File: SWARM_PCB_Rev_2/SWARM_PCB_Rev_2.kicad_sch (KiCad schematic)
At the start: 4 parts, among them J25 Conn_01x12_Pin, J26 Conn_01x12_Pin, J27 Conn_01x12_Pin, J28 Conn_01x13_Pin

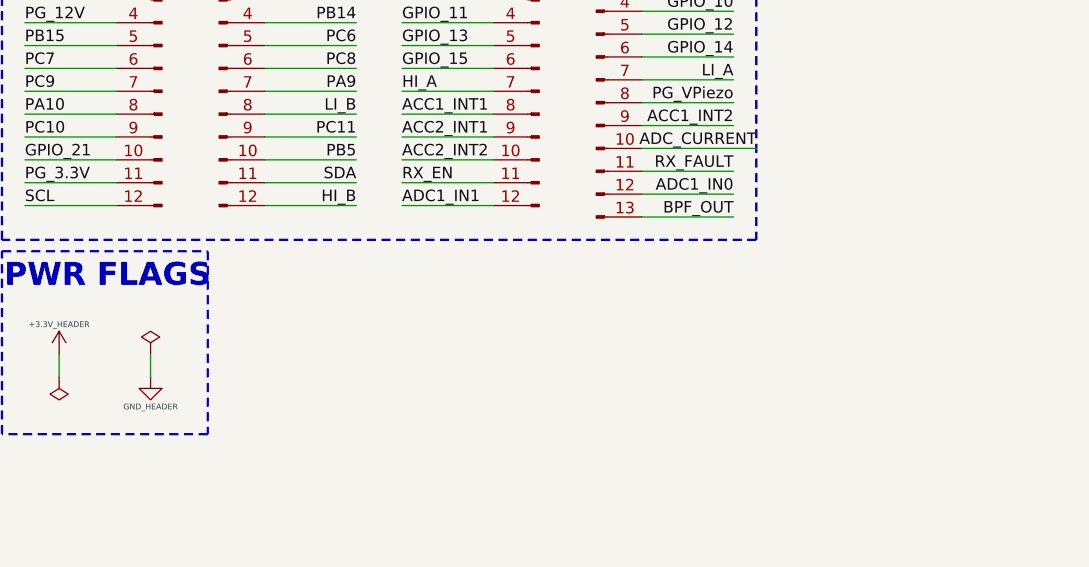
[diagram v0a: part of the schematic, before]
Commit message: Design review fixes: feedback resistor, SWCLK, LED MPNs, GND annotation
- POWER: correct bR10 feedback resistor 187k→255k so TPS55340RTER
  (Vref=0.9V) sets VPiezo to 23.85V (~24V target)
- POWER: assign MPNs for bD2 (green), bD3/bD4 (blue) JE2835 LEDs
- CONTROL: add 33Ω series resistor aR18 on SWCLK near debug header aJ4
- CONTROL: assign MPNs for aD1 (purple) and aD2 (RGB) LEDs
- Top schematic: document isolated GND domain architecture (H3)
- PCB layout, sub-sheet, and SPICE updates

Co-Authored-By: Claude Sonnet 4.6 <noreply@anthropic.com>
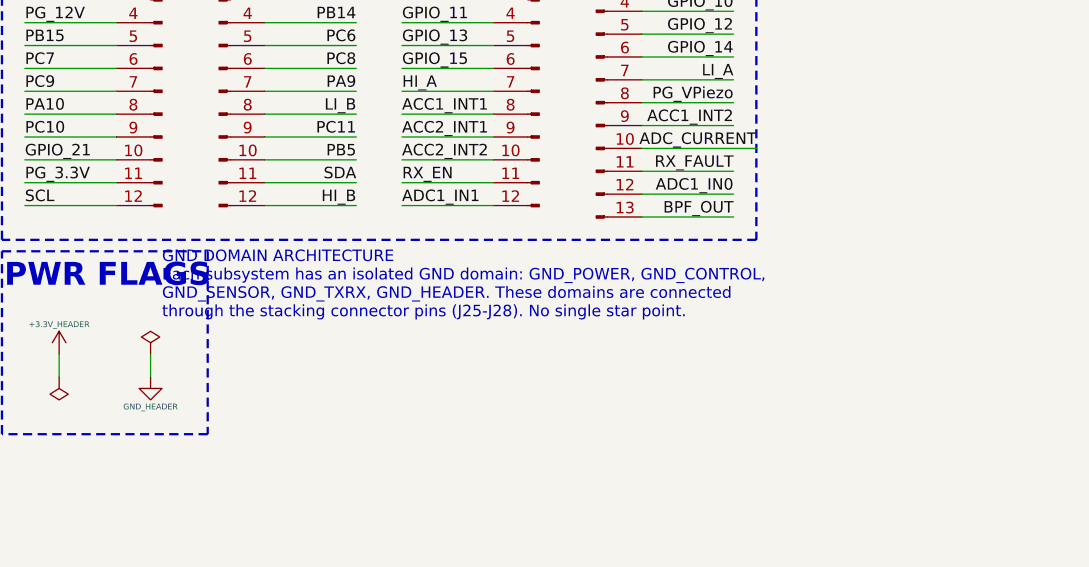
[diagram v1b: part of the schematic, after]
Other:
- note added: "GND DOMAIN ARCHITECTURE Each subsystem has an isolated GND domain: GND_POWER, GND_CONTROL, GND_SENSOR, GND_TXRX, GND_HEADER. These domains are connected through the stacking connector pins (J25-J28). No single star point."
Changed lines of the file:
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@@
+		)
+	)
+	(text "GND DOMAIN ARCHITECTURE\nEach subsystem has an isolated GND domain: GND_POWER, GND_CONTROL,\nGND_SENSOR, GND_TXRX, GND_HEADER. These domains are connected\nthrough the stacking connector pins (J25-J28). No single star point."
+		(exclude_from_sim no)
+		(at 82.55 62.23 0)
+		(effects
+			(font
+				(size 1.27 1.27)
+			)
+			(justify left)
 		)
 	)
